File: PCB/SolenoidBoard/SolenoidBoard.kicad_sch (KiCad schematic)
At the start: 0 parts

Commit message: コネクタ配置
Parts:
- added C1, C2: C_Small_US, symbol Device:C_Small_US
- added D1: LED_Small, symbol Device:LED_Small
- added J1, J2: Conn_01x02_Pin, symbol Connector:Conn_01x02_Pin
- added R1: R_Small, symbol Device:R_Small
- added S1: SKRPACE010, SKRPACE010:SW_SKRPACE010, symbol SKRPACE010:SKRPACE010

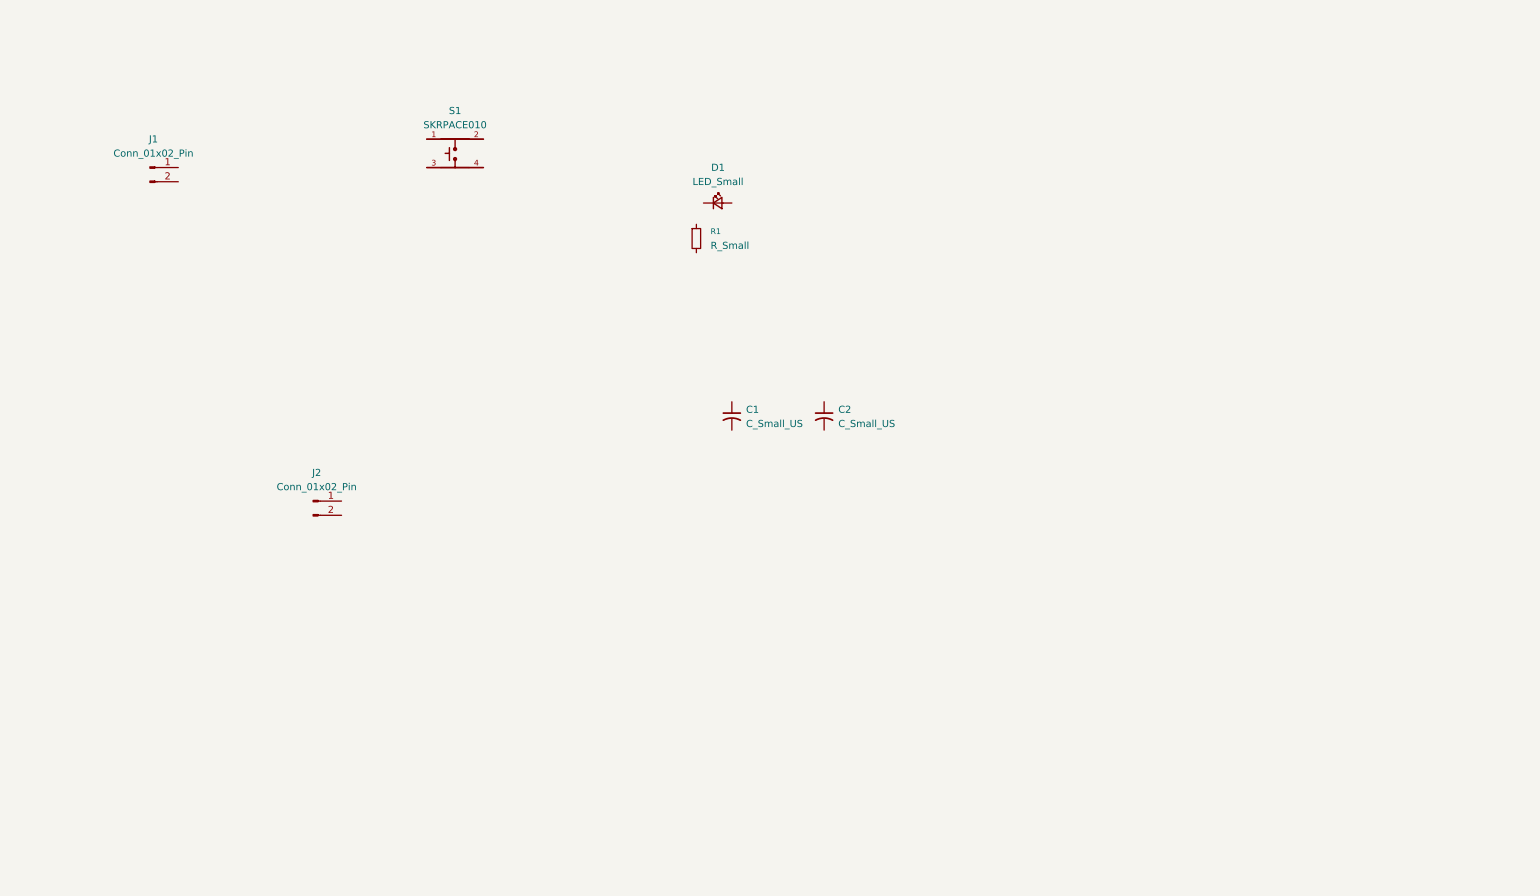
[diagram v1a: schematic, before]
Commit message: 昇圧部コピー
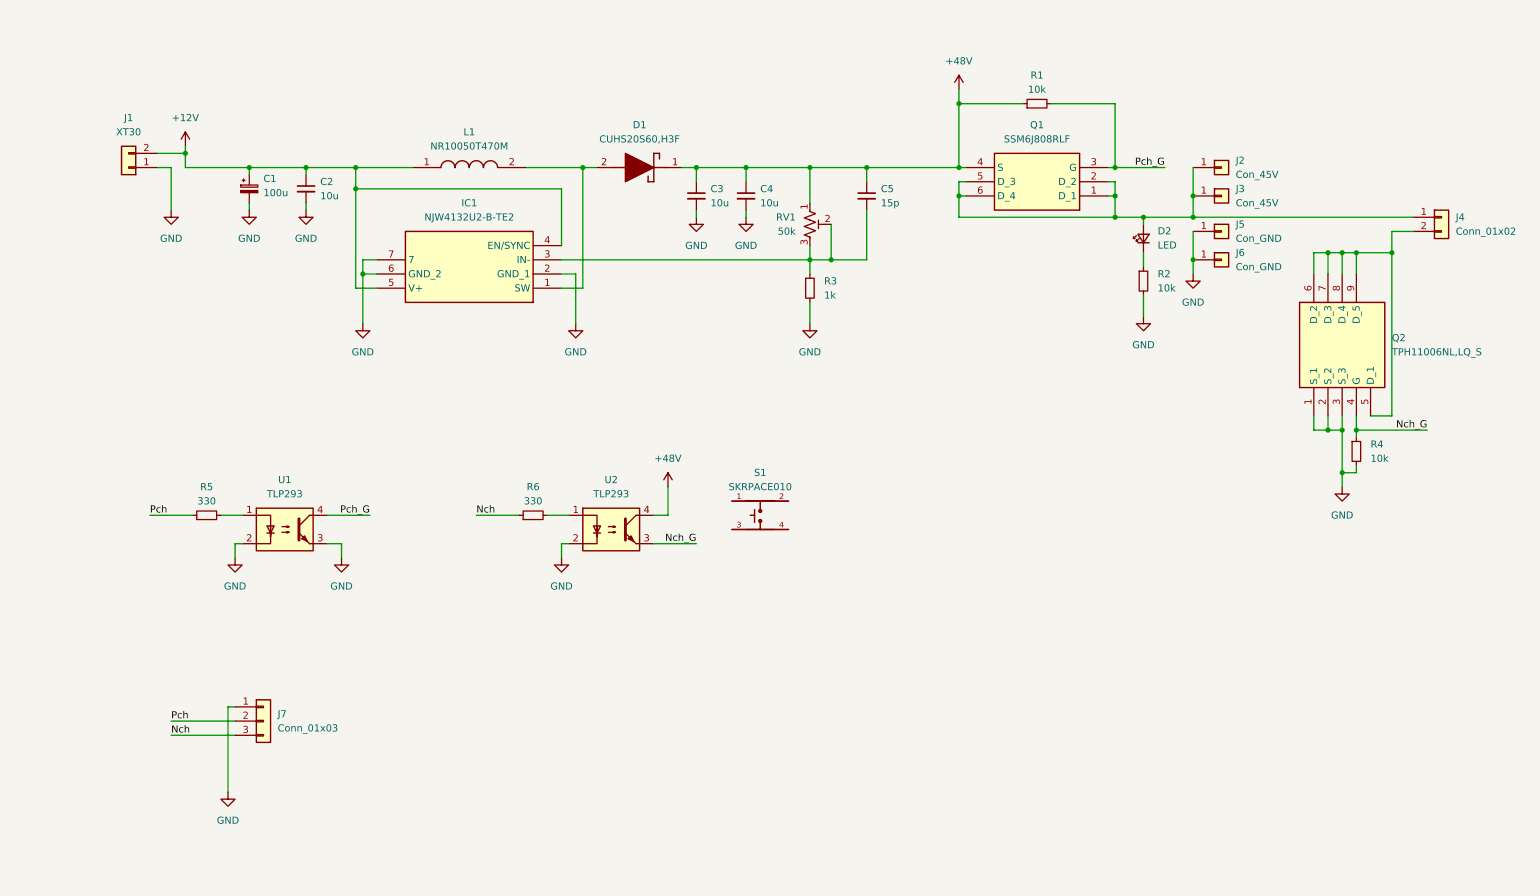
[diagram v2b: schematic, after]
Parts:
- removed C1, C2: C_Small_US, symbol Device:C_Small_US
- removed D1: LED_Small, symbol Device:LED_Small
- removed J1, J2: Conn_01x02_Pin, symbol Connector:Conn_01x02_Pin
- added C1: 100u, Capacitor_SMD:CP_Elec_8x10, symbol Device:C_Polarized_Small
- added C2, C3, C4: 10u, Capacitor_SMD:C_1210_3225Metric, symbol Device:C_Small
- added C5: 15p, Capacitor_SMD:C_0603_1608Metric, symbol Device:C_Small
- added D1: CUHS20S60,H3F, CUHS20S60,H3F:CUHS20S60H3F, symbol CUHS20S60_H3F:CUHS20S60,H3F
- added D2: LED, LED_SMD:LED_0603_1608Metric, symbol Device:LED_Small
- added IC1: NJW4132U2-B-TE2, NJW4132U2-B-TE2:NJW4132U2BTE2, symbol NJW4132U2-B-TE2:NJW4132U2-B-TE2
- added J1: XT30, Connector_AMASS:AMASS_XT30PW-M_1x02_P2.50mm_Horizontal, symbol Connector_Generic:Conn_01x02
- added J2, J3: Con_45V, Connector_PinSocket_2.54mm:PinSocket_1x01_P2.54mm_Vertical, symbol Connector_Generic:Conn_01x01
- added J4: Conn_01x02, Connector_JST:JST_XA_S02B-XASK-1_1x02_P2.50mm_Horizontal, symbol Connector_Generic:Conn_01x02
- added J5, J6: Con_GND, Connector_PinSocket_2.54mm:PinSocket_1x01_P2.54mm_Vertical, symbol Connector_Generic:Conn_01x01
- added J7: Conn_01x03, Connector_JST:JST_PH_S3B-PH-K_1x03_P2.00mm_Horizontal, symbol Connector_Generic:Conn_01x03
- added L1: NR10050T470M, NR10050T470M:NR10050T470M, symbol NR10050T470M:NR10050T470M
- added Q1: SSM6J808RLF, SSM6J808RLF:SSM6J808RLF, symbol SSM6J808RLF:SSM6J808RLF
- added Q2: TPH11006NL,LQ_S, TPH11006NL,LQ_S:TPH11006NLLQS, symbol TPH11006NL_LQ_S:TPH11006NL,LQ_S
- added R2, R4: 10k, Resistor_SMD:R_0603_1608Metric, symbol Device:R_Small
- added R3: 1k, Resistor_SMD:R_0603_1608Metric, symbol Device:R_Small
- added R5, R6: 330, Resistor_SMD:R_0603_1608Metric, symbol Device:R_Small
- added RV1: 50k, TC33X:TC33X2503E, symbol Device:R_Potentiometer_Trim_US
- added U1, U2: TLP293, Package_SO:SOIC-4_4.55x2.6mm_P1.27mm, symbol Isolator:TLP293
- R1: value R_Small -> 10k; footprint (none) -> Resistor_SMD:R_0603_1608Metric
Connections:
- net +48V: now reaches R1.1
- net +48V: now also C3.1, C4.1, C5.1, D1.1 (K), Q1.4 (S), RV1.1, U2.4
- net Pch_G: now reaches R1.2
- net Pch_G: now also Q1.3 (G), U1.4
- new net: C5.2, IC1.3 (IN-), R3.1, RV1.2, RV1.3
- new net: D2.2 (A), J2.1 (Pin_1), J3.1 (Pin_1), J4.1 (Pin_1), Q1.1 (D_1), Q1.2 (D_2), Q1.5 (D_3), Q1.6 (D_4)
- new net: J4.2 (Pin_2), Q2.5 (D_1), Q2.6 (D_2), Q2.7 (D_3), Q2.8 (D_4), Q2.9 (D_5)
- new net: R6.2, U2.1
- new net: D2.1 (K), R2.1
- new net: D1.2 (A), IC1.1 (SW), L1.2
- new net: R5.2, U1.1
- new net +12V: C1.1, C2.1, IC1.4 (EN/SYNC), IC1.5 (V+), J1.2 (Pin_2), L1.1
- new net GND: C1.2, C2.2, C3.2, C4.2, IC1.2 (GND_1), IC1.6 (GND_2), IC1.7, J1.1 (Pin_1), J5.1 (Pin_1), J6.1 (Pin_1), J7.1 (Pin_1), Q2.1 (S_1), Q2.2 (S_2), Q2.3 (S_3), R2.2, R3.2, R4.2, U1.2, U1.3, U2.2
- new net Nch: J7.3 (Pin_3), R6.1
- new net Nch_G: Q2.4 (G), R4.1, U2.3
- new net Pch: J7.2 (Pin_2), R5.1
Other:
- moved on the sheet: S1

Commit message: 回路図完成
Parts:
- removed J7: Conn_01x03, Connector_JST:JST_PH_S3B-PH-K_1x03_P2.00mm_Horizontal, symbol Connector_Generic:Conn_01x03
- removed Q1: SSM6J808RLF, SSM6J808RLF:SSM6J808RLF, symbol SSM6J808RLF:SSM6J808RLF
- removed Q2: TPH11006NL,LQ_S, TPH11006NL,LQ_S:TPH11006NLLQS, symbol TPH11006NL_LQ_S:TPH11006NL,LQ_S
- removed R4: 10k, Resistor_SMD:R_0603_1608Metric, symbol Device:R_Small
- removed S1: SKRPACE010, SKRPACE010:SW_SKRPACE010, symbol SKRPACE010:SKRPACE010
- added F1: 3557-15, 3557-15:FUSE_3557-15, symbol 3557-15:3557-15
- added J7, J9: Conn_01x02, Connector_JST:JST_XA_S02B-XASK-1_1x02_P2.50mm_Horizontal, symbol Connector_Generic:Conn_01x02
- added J8: Conn_01x06_Pin, symbol Connector:Conn_01x06_Pin
- added Q1: Q_PMOS_GSD, Package_TO_SOT_SMD:SOT-23-3, symbol Transistor_FET:Q_PMOS_GSD
- added Q3, Q4, Q5: TPH11006NL,LQ_S, SOP Advance:SOP Advance, symbol TPH11006NL_LQ_S:TPH11006NL,LQ_S
- added R10, R11, R9: 10k, Resistor_SMD:R_0603_1608Metric, symbol Device:R_Small
- added R7, R8: 330, Resistor_SMD:R_0603_1608Metric, symbol Device:R_Small
- added U3, U4: TLP293, Package_SO:SOIC-4_4.55x2.6mm_P1.27mm, symbol Isolator:TLP293
- D1: footprint CUHS20S60,H3F:CUHS20S60H3F -> Diode_SMD:D_SOD-323_HandSoldering
- IC1: footprint NJW4132U2-B-TE2:NJW4132U2BTE2 -> Package_TO_SOT_SMD:SOT-89-5_Handsoldering
- L1: footprint NR10050T470M:NR10050T470M -> Inductor_SMD:L_10.4x10.4_H4.8
- RV1: footprint TC33X:TC33X2503E -> Potentiometer_SMD:Potentiometer_Bourns_TC33X_Vertical
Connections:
- net +12V: now also F1.2_1, F1.2_2; no longer J1.2 (Pin_2)
- net +48V: now also Q1.2 (S), U3.4, U4.4
- net GND: now also J8.1 (Pin_1), Q3.1 (S_1), Q3.2 (S_2), Q3.3 (S_3), Q4.1 (S_1), Q4.2 (S_2), Q4.3 (S_3), Q5.1 (S_1), Q5.2 (S_2), Q5.3 (S_3), R10.2, R11.2, R9.2, U3.2, U4.2
- net Pch: now also J8.3 (Pin_3)
- net Pch_G: now also Q1.1 (G)
- net at D2.2 (A), J2.1 (Pin_1), J3.1 (Pin_1)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: now also J7.1 (Pin_1), J9.1 (Pin_1), Q1.3 (D)
- net at J4.2 (Pin_2): now also Q5.5 (D_1), Q5.6 (D_2), Q5.7 (D_3), Q5.8 (D_4), Q5.9 (D_5)
- net Nch renamed Nch_R
- net Nch_R: now also J8.4 (Pin_4)
- net Nch_G renamed Nch_R_G
- net Nch_R_G: now also Q5.4 (G), R11.1
- new net: R7.2, U3.1
- new net: F1.1_1, F1.1_2, J1.2 (Pin_2)
- new net: J9.2 (Pin_2), Q4.5 (D_1), Q4.6 (D_2), Q4.7 (D_3), Q4.8 (D_4), Q4.9 (D_5)
- new net: J7.2 (Pin_2), Q3.5 (D_1), Q3.6 (D_2), Q3.7 (D_3), Q3.8 (D_4), Q3.9 (D_5)
- new net: R8.2, U4.1
- new net Nch_C: J8.5 (Pin_5), R7.1
- new net Nch_C_G: Q3.4 (G), R9.1, U3.3
- new net Nch_L: J8.6 (Pin_6), R8.1
- new net Nch_L_G: Q4.4 (G), R10.1, U4.3
- no-connect marks 0 -> 1
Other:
- moved on the sheet: C1, C2, C3, C4, C5, D1, D2, IC1, J1, J2, J3, J4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
